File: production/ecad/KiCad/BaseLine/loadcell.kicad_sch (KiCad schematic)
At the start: 13 parts, among them J4 LoadCellConnector, U6 MIC920YC5-TR, U7 MIC920YC5-TR, U8 ADS1231IDR

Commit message: More updated annotations and stuff
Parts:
- renumbered R32 to R35, R33 to R36, R34 to R37, R35 to R38
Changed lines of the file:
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@@
 		(on_board yes)
 		(dnp no)
-		(property "Reference" "R34"
+		(property "Reference" "R37"
 			(at 50.546 175.514 90)
 			(effects
@@
 			(project "BaseLine"
 				(path "/ba9eda21-3882-41e1-8265-3d8ac781da20/15451660-bad9-4e79-85d3-2d59df8c5ccd"
-					(reference "R34")
+					(reference "R37")
 					(unit 1)
 				)
@@
 		(dnp no)
 		(fields_autoplaced yes)
-		(property "Reference" "R32"
+		(property "Reference" "R35"
 			(at 36.83 135.89 90)
 			(effects
@@
 			(project "BaseLine"
 				(path "/ba9eda21-3882-41e1-8265-3d8ac781da20/15451660-bad9-4e79-85d3-2d59df8c5ccd"
-					(reference "R32")
+					(reference "R35")
 					(unit 1)
 				)
@@
 		(dnp no)
 		(fields_autoplaced yes)
-		(property "Reference" "R35"
+		(property "Reference" "R38"
 			(at 53.34 135.89 90)
 			(effects
@@
 			(project "BaseLine"
 				(path "/ba9eda21-3882-41e1-8265-3d8ac781da20/15451660-bad9-4e79-85d3-2d59df8c5ccd"
-					(reference "R35")
+					(reference "R38")
 					(unit 1)
 				)
@@
 		(on_board yes)
 		(dnp no)
-		(property "Reference" "R33"
+		(property "Reference" "R36"
 			(at 40.64 175.26 90)
 			(effects
@@
 			(project "BaseLine"
 				(path "/ba9eda21-3882-41e1-8265-3d8ac781da20/15451660-bad9-4e79-85d3-2d59df8c5ccd"
-					(reference "R33")
-					(unit 1)
-				)
+					(reference "R36")
+					(unit 1)
+				)

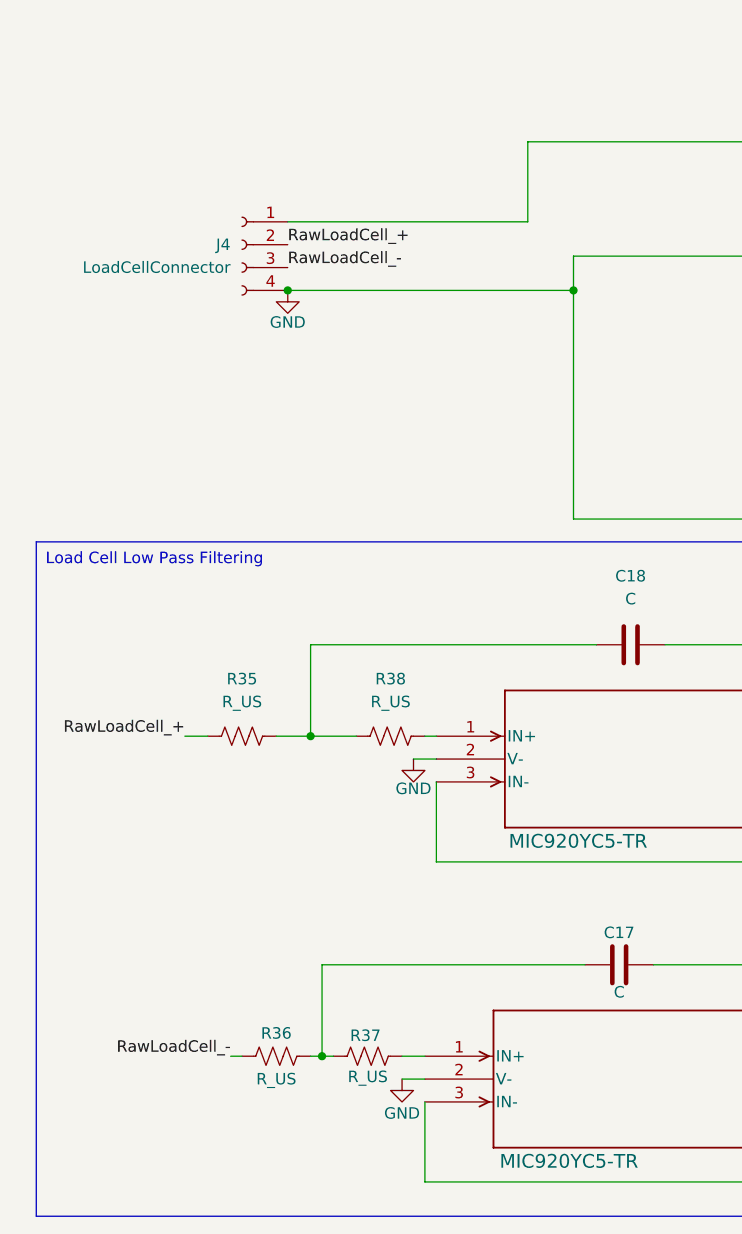
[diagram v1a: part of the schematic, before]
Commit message: Added test points
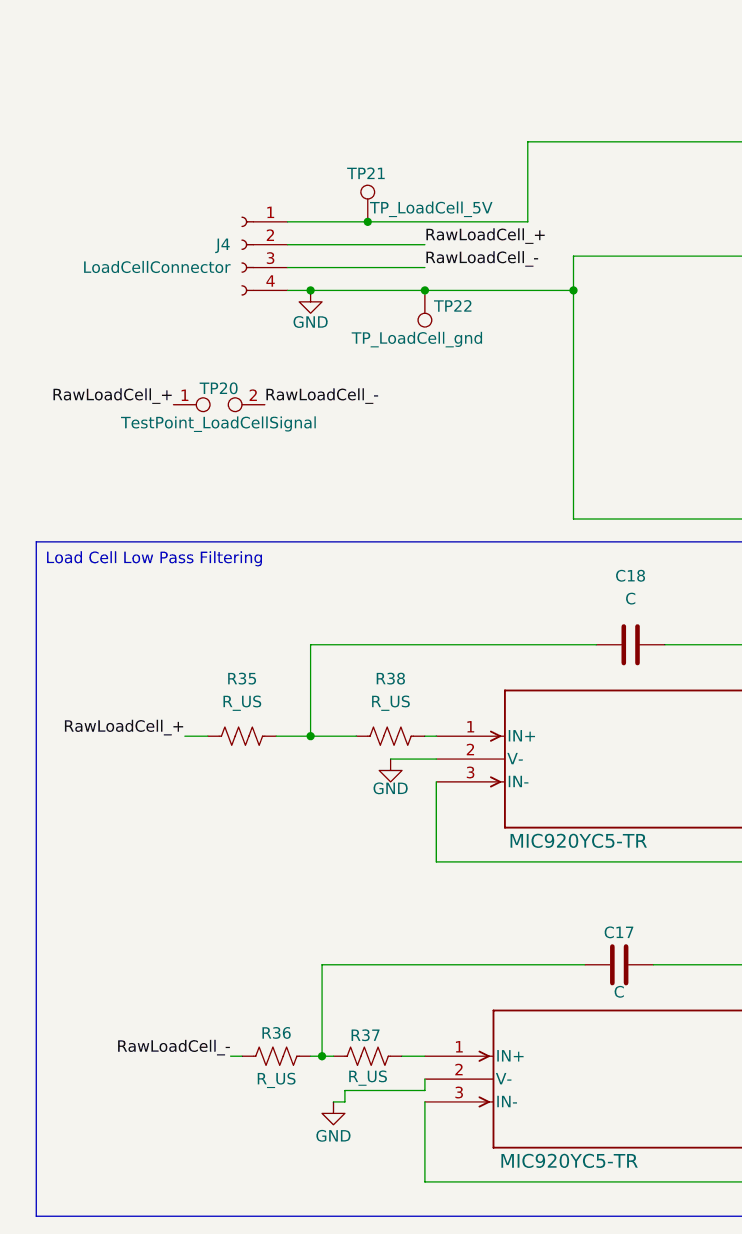
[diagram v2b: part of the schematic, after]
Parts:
- added TP20: TestPoint_LoadCellSignal, symbol Connector:TestPoint_2Pole
- added TP21: TP_LoadCell_5V, symbol Connector:TestPoint
- added TP22: TP_LoadCell_gnd, symbol Connector:TestPoint
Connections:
- net +5V: now also TP21.1
- net GND: now also TP22.1
- net RawLoadCell_+: now also TP20.1
- net RawLoadCell_-: now also TP20.2

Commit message: Sean DR updates
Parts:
- removed R37, R38: R_US, symbol Device:R_US
- C18: value C -> VAR
- R35, R36: value R_US -> VAR
- renumbered C17 to VAR
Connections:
- net GND: now also C18.2, VAR.2; no longer J4.4 (Pin_4), TP22.1, U8.12 (SW), U8.9 (VREFN)
- net LP_+: no longer C18.2
- net LP_-: no longer VAR.2
- net at U6.1 (IN+): now also R36.1, VAR.1
- net at C18.1, R35.1: now also U7.1 (IN+)
- new net: J4.4 (Pin_4), TP22.1, U8.12 (SW), U8.9 (VREFN)
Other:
- moved on the sheet: C18, C19, R36, TP21, TP22, VAR

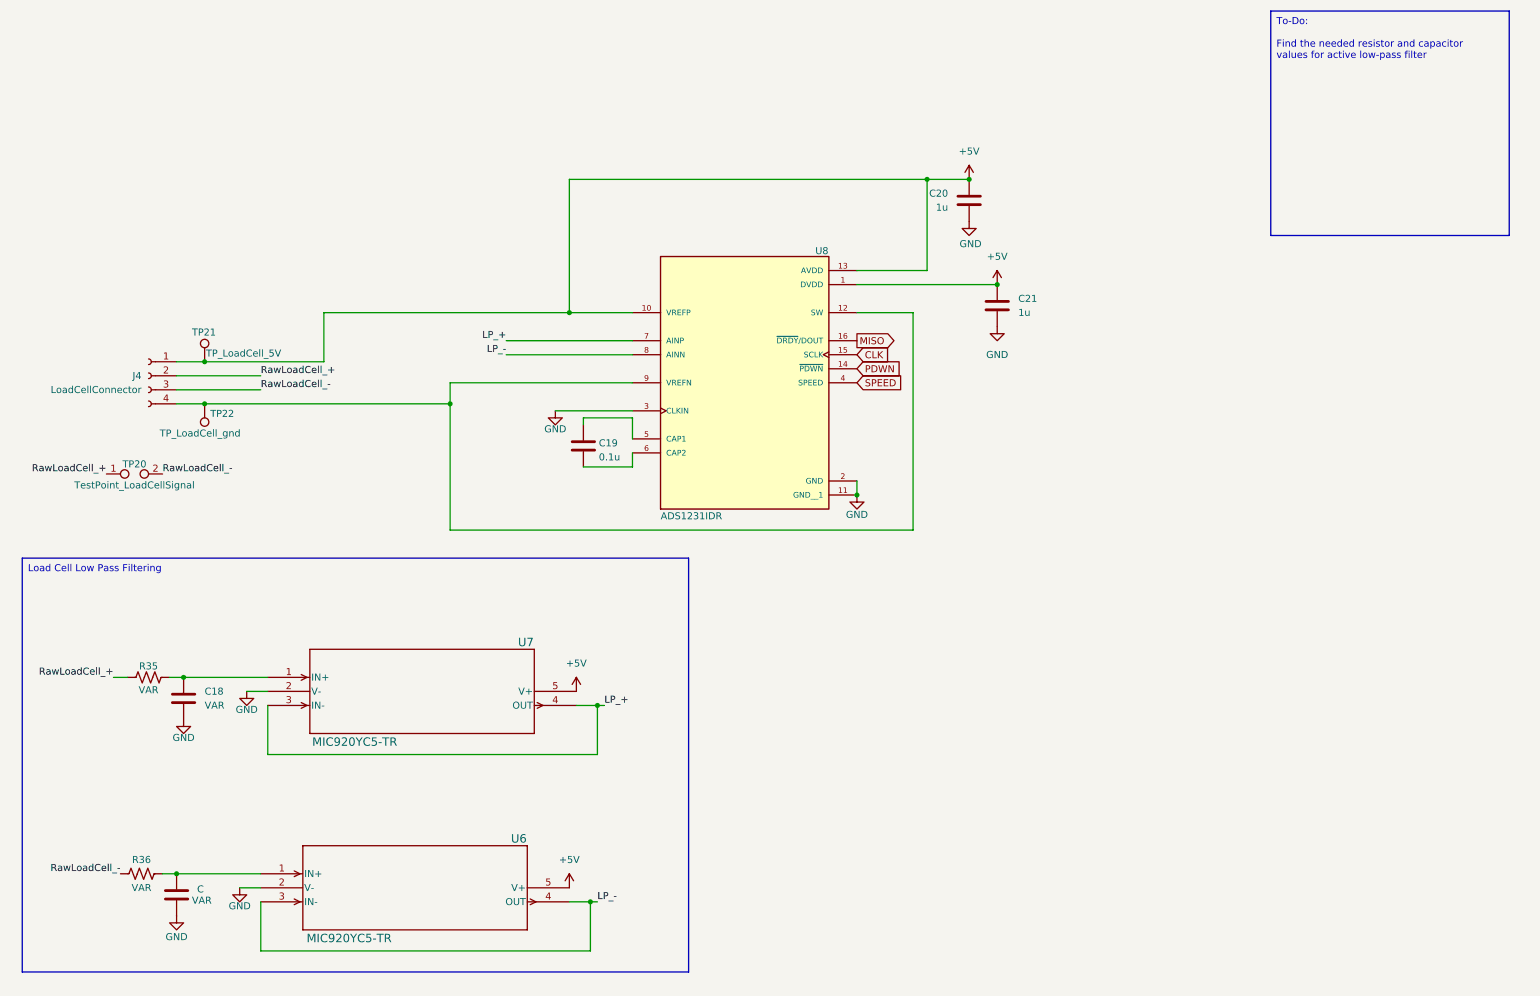
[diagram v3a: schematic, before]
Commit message: Added mux to mcu and fix-ups
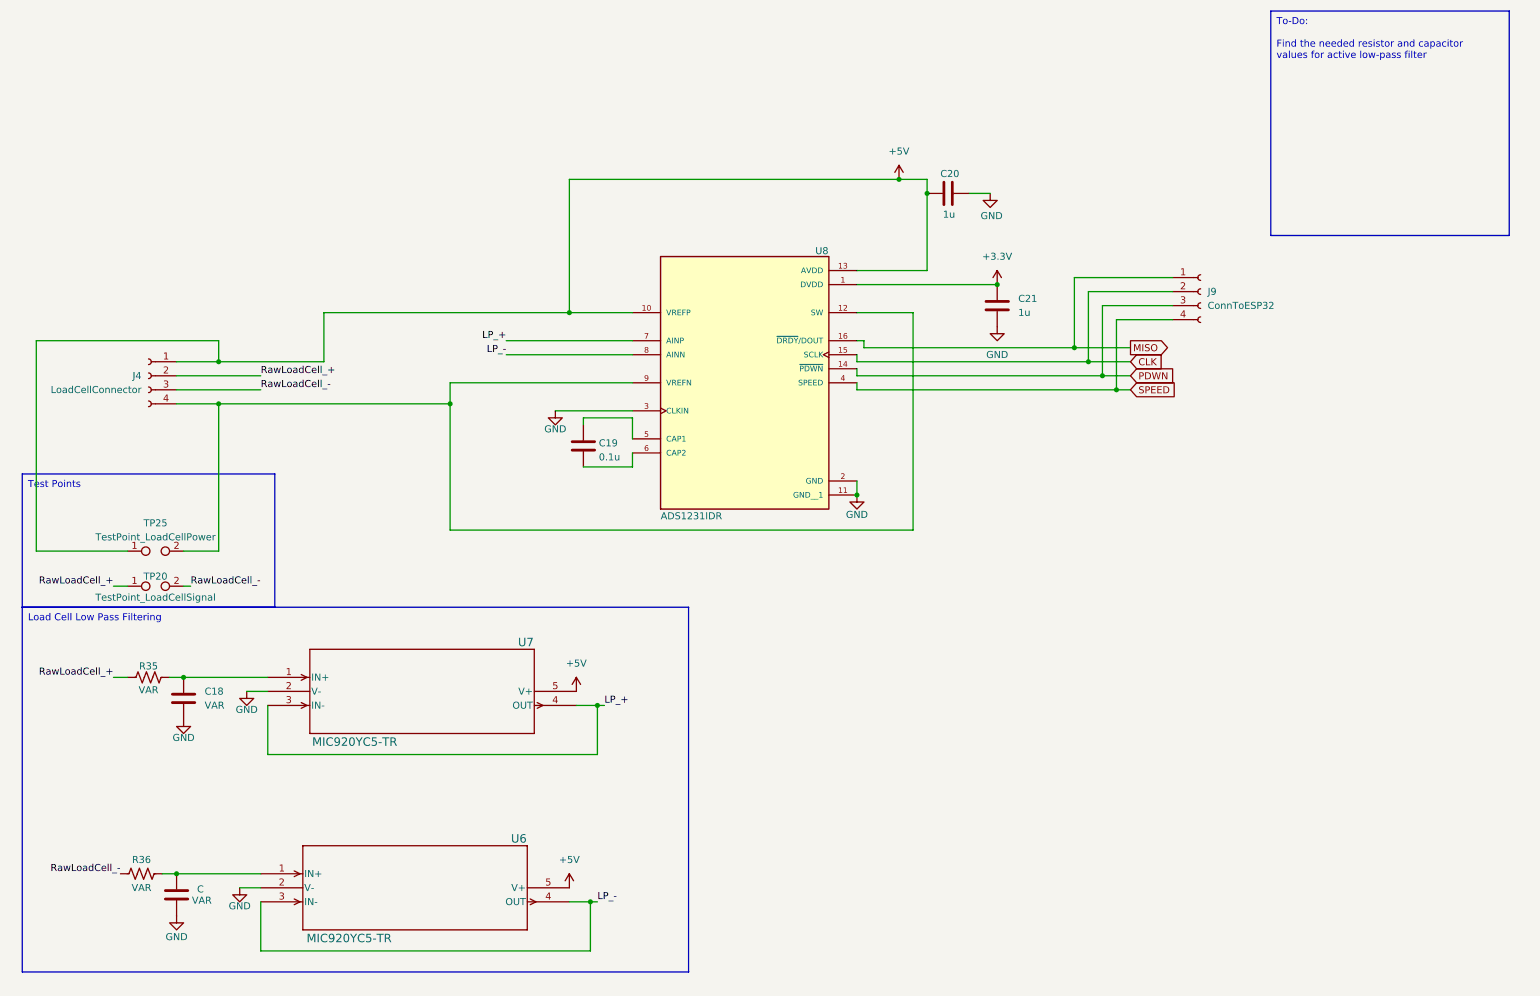
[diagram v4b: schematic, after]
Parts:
- removed TP21: TP_LoadCell_5V, symbol Connector:TestPoint
- removed TP22: TP_LoadCell_gnd, symbol Connector:TestPoint
- added J9: ConnToESP32, symbol Connector:Conn_01x04_Socket
- added TP25: TestPoint_LoadCellPower, symbol Connector:TestPoint_2Pole
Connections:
- net +5V: now also TP25.1; no longer C21.1, U8.1 (DVDD)
- net CLK: now also J9.2 (Pin_2)
- net MISO: now also J9.1 (Pin_1)
- net PDWN: now also J9.3 (Pin_3)
- net SPEED: now also J9.4 (Pin_4)
- net at J4.4 (Pin_4), U8.12 (SW), U8.9 (VREFN): now also TP25.2
- new net +3.3V: C21.1, U8.1 (DVDD)
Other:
- moved on the sheet: C20, TP20

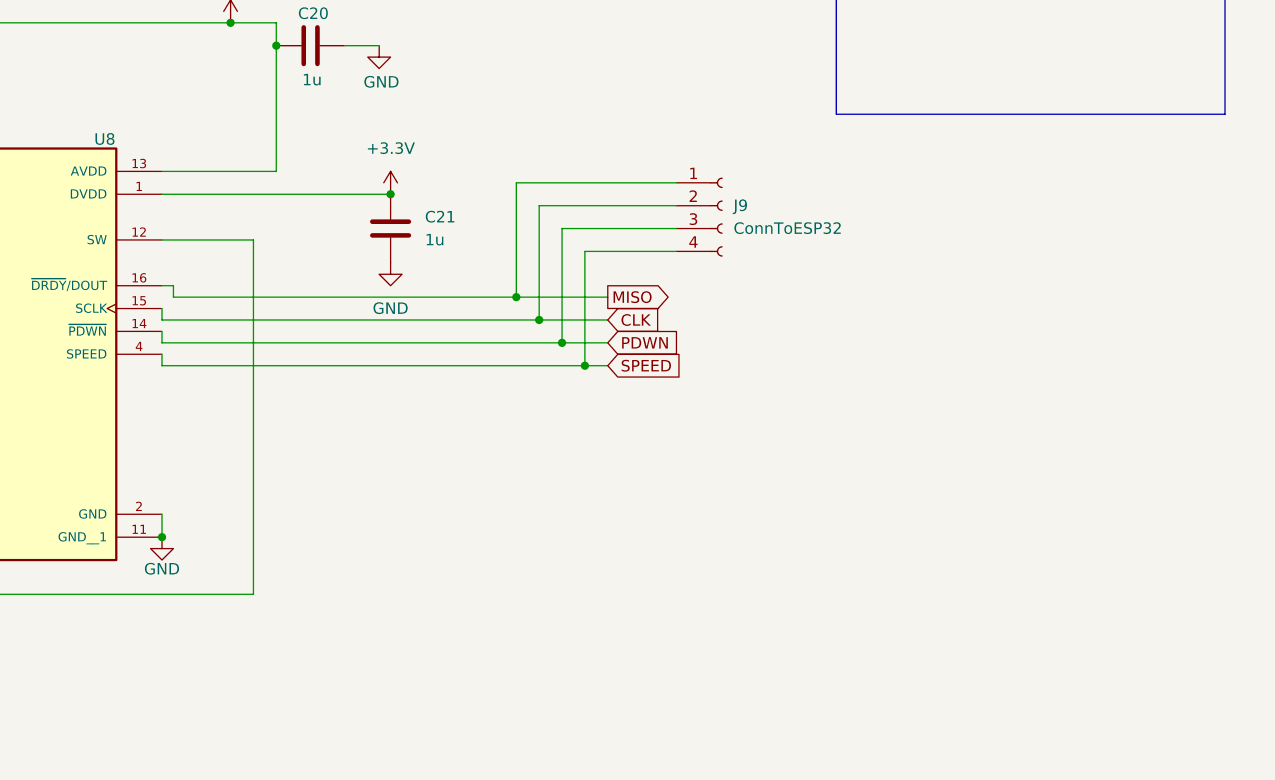
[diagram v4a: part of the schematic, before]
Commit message: Added level shifter to load cell
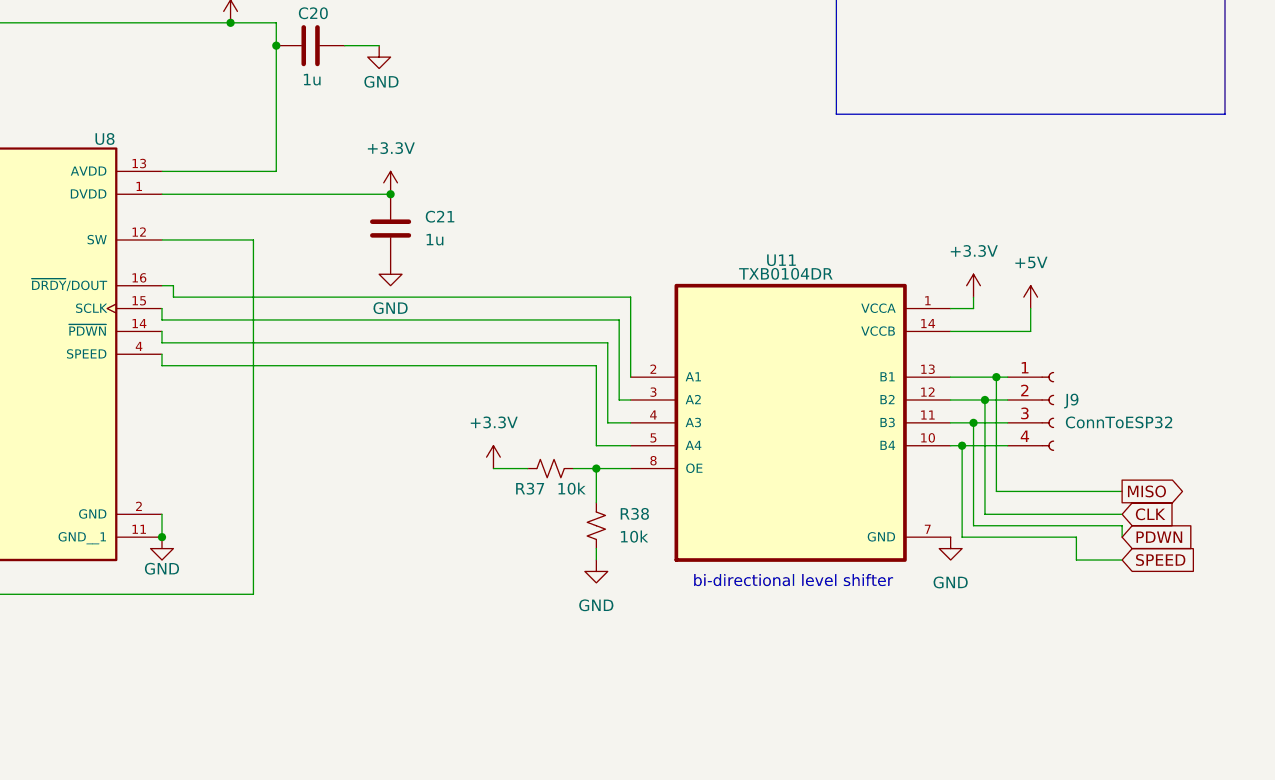
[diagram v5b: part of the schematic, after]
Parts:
- added R37, R38: 10k, symbol Device:R_Small_US
- added U11: TXB0104DR, TXB0104DR:SOIC127P600X175-14N, symbol TXB0104DR:TXB0104DR
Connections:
- net +3.3V: now also R37.1, U11.1 (VCCA)
- net +5V: now also U11.14 (VCCB)
- net CLK: now also U11.12 (B2); no longer U8.15 (SCLK)
- net GND: now also R38.2, U11.7 (GND)
- net MISO: now also U11.13 (B1); no longer U8.16 (~{DRDY}/DOUT)
- net PDWN: now also U11.11 (B3); no longer U8.14 (~{PDWN})
- net SPEED: now also U11.10 (B4); no longer U8.4 (SPEED)
- new net: R37.2, R38.1, U11.8 (OE)
- new net: U11.2 (A1), U8.16 (~{DRDY}/DOUT)
- new net: U11.3 (A2), U8.15 (SCLK)
- new net: U11.4 (A3), U8.14 (~{PDWN})
- new net: U11.5 (A4), U8.4 (SPEED)
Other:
- note added: "bi-directional level shifter"
- moved on the sheet: J9
